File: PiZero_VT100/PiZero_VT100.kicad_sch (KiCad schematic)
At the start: 24 parts, among them J1 GPIO, J2 RS232, J3 Ext. Power max,. 9V DC/AC, J4 Mini-DIN-6, J5 to Testpins 22(DM) and TP23(D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, J6 USB_A, J7 Z80-MBC2 direct, U2 LM7805_TO220

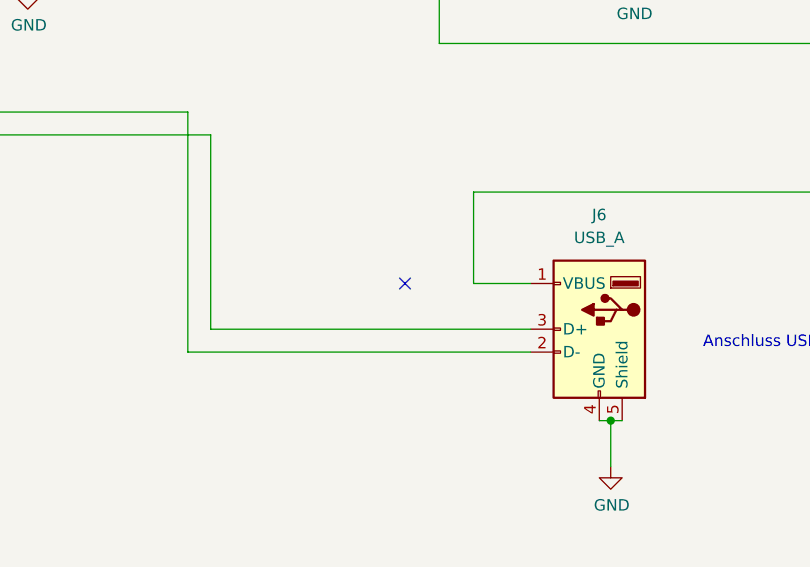
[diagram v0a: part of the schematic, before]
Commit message: Geänderte Adapterplatine mit Readme
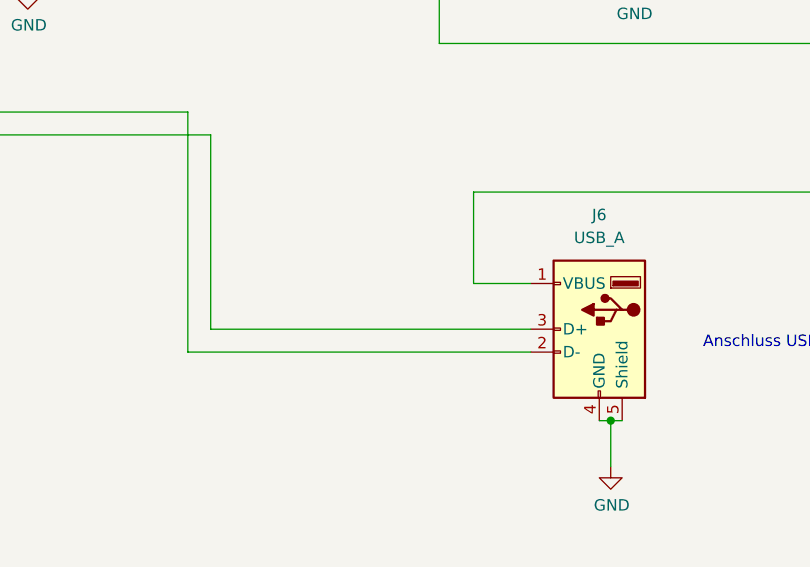
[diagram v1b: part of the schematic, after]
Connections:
- no-connect marks 36 -> 35
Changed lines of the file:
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@@
-	)
-	(no_connect
-		(at 199.39 125.73)
 	)
 	(no_connect

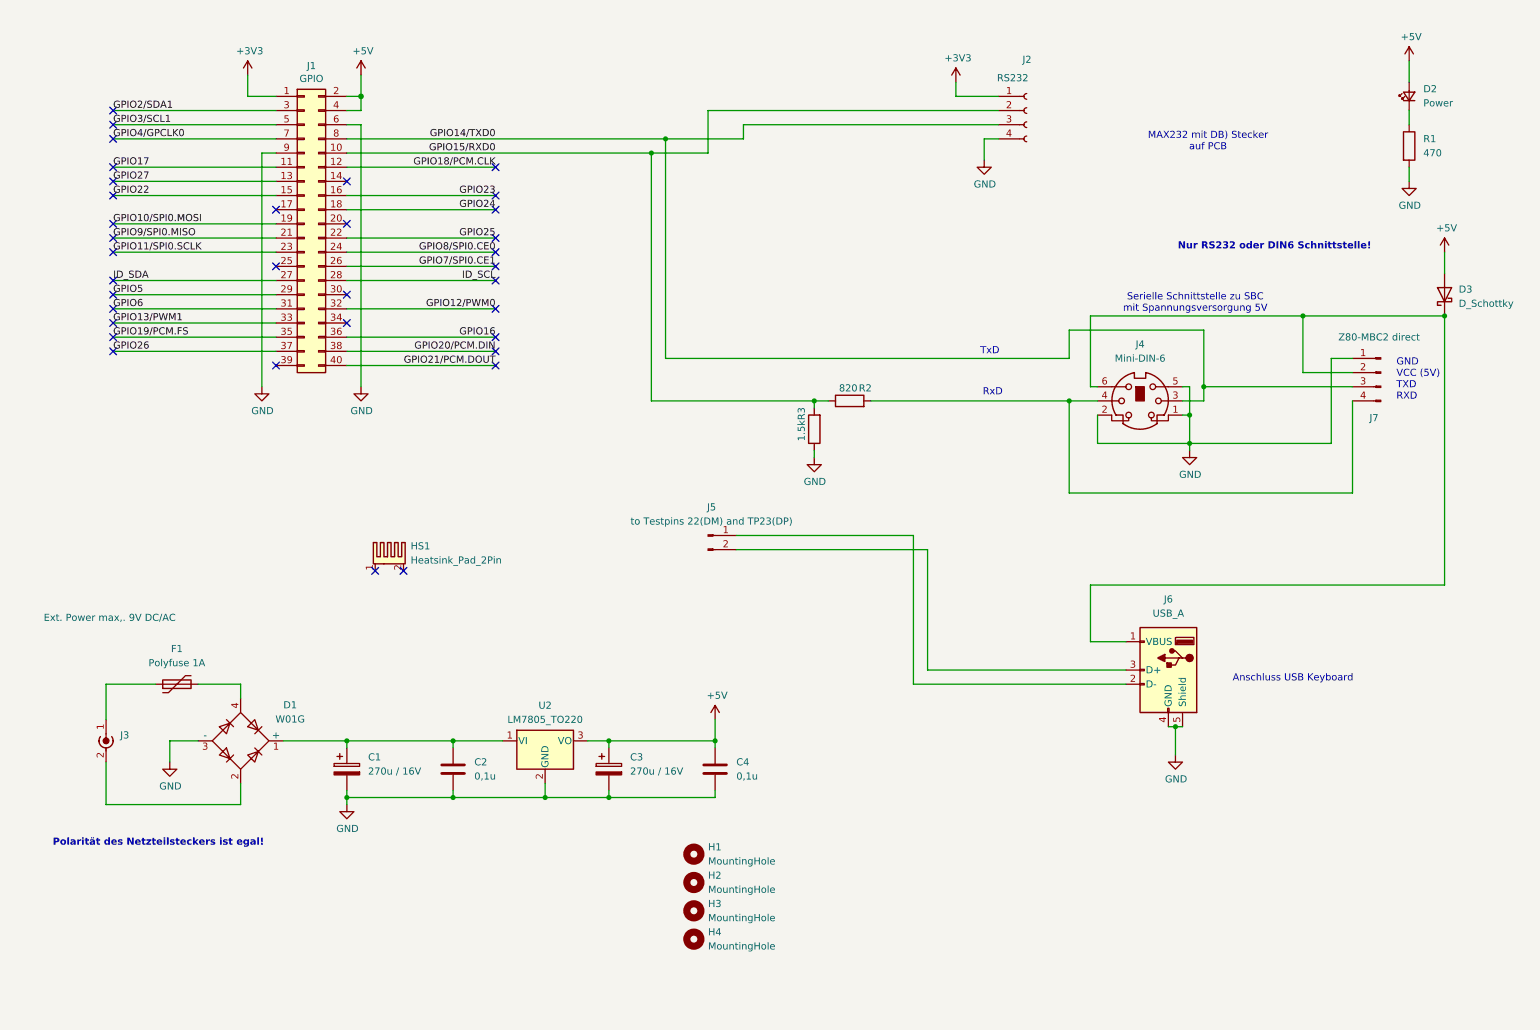
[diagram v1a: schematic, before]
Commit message: Schaltung aktualisiert Umschaltung RxD <> TxD fehlt noch
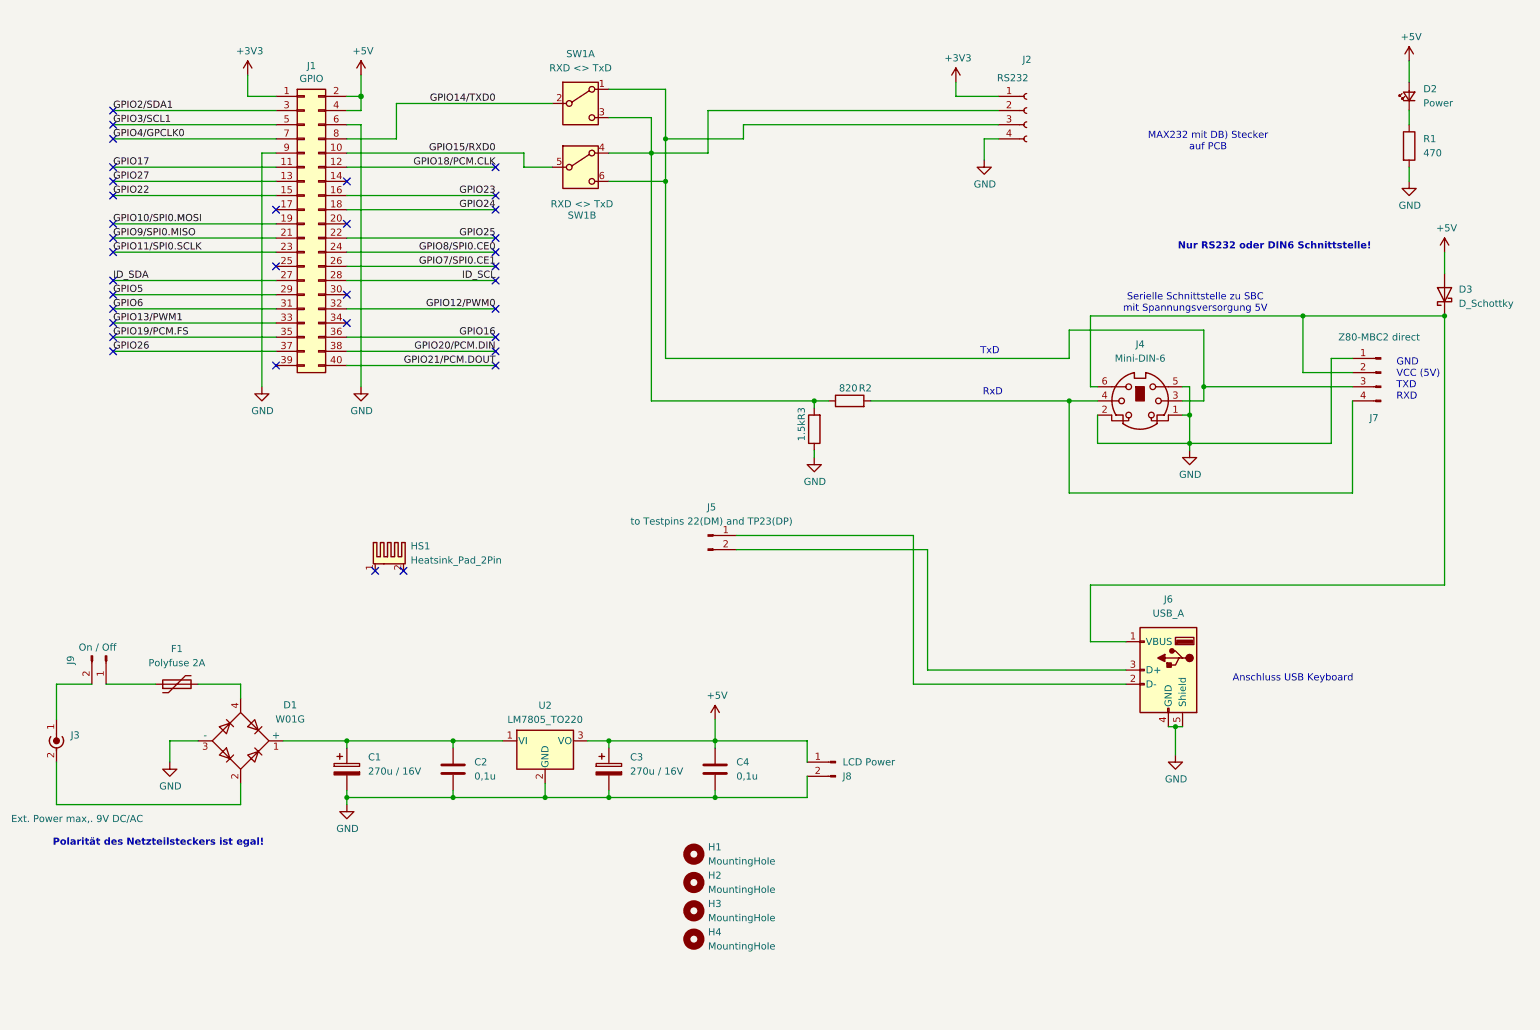
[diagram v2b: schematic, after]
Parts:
- added J8: LCD Power, Connector_PinHeader_2.54mm:PinHeader_1x02_P2.54mm_Vertical, symbol Connector:Conn_01x02_Pin
- added J9: On / Off, Connector_PinHeader_2.54mm:PinHeader_1x02_P2.54mm_Vertical, symbol Connector:Conn_01x02_Pin
- added SW1: RXD <> TxD, Button_Switch_THT:SW_CK_JS202011AQN_DPDT_Angled, symbol Switch:SW_DPDT_x2
- F1: value Polyfuse 1A -> Polyfuse 2A
- J3: footprint Connector_PinHeader_2.54mm:PinHeader_1x02_P2.54mm_Vertical -> Connector_BarrelJack:BarrelJack_GCT_DCJ200-10-A_Horizontal
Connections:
- net +5V: now also J8.1 (Pin_1)
- net GND: now also J8.2 (Pin_2)
- net GPIO14/TXD0: now also SW1.2 (B); no longer J2.3 (Pin_3), J4.3, J7.3 (Pin_3)
- net GPIO15/RXD0: now also SW1.5 (B); no longer J2.2 (Pin_2), R2.1, R3.2
- net at F1.1: now also J9.1 (Pin_1); no longer J3.1 (In)
- new net: J2.2 (Pin_2), R2.1, R3.2, SW1.3 (C), SW1.4 (A)
- new net: J2.3 (Pin_3), J4.3, J7.3 (Pin_3), SW1.1 (A), SW1.6 (C)
- new net: J3.1 (In), J9.2 (Pin_2)
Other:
- moved on the sheet: J3

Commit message: Umschalter TxD / RxD über Relais
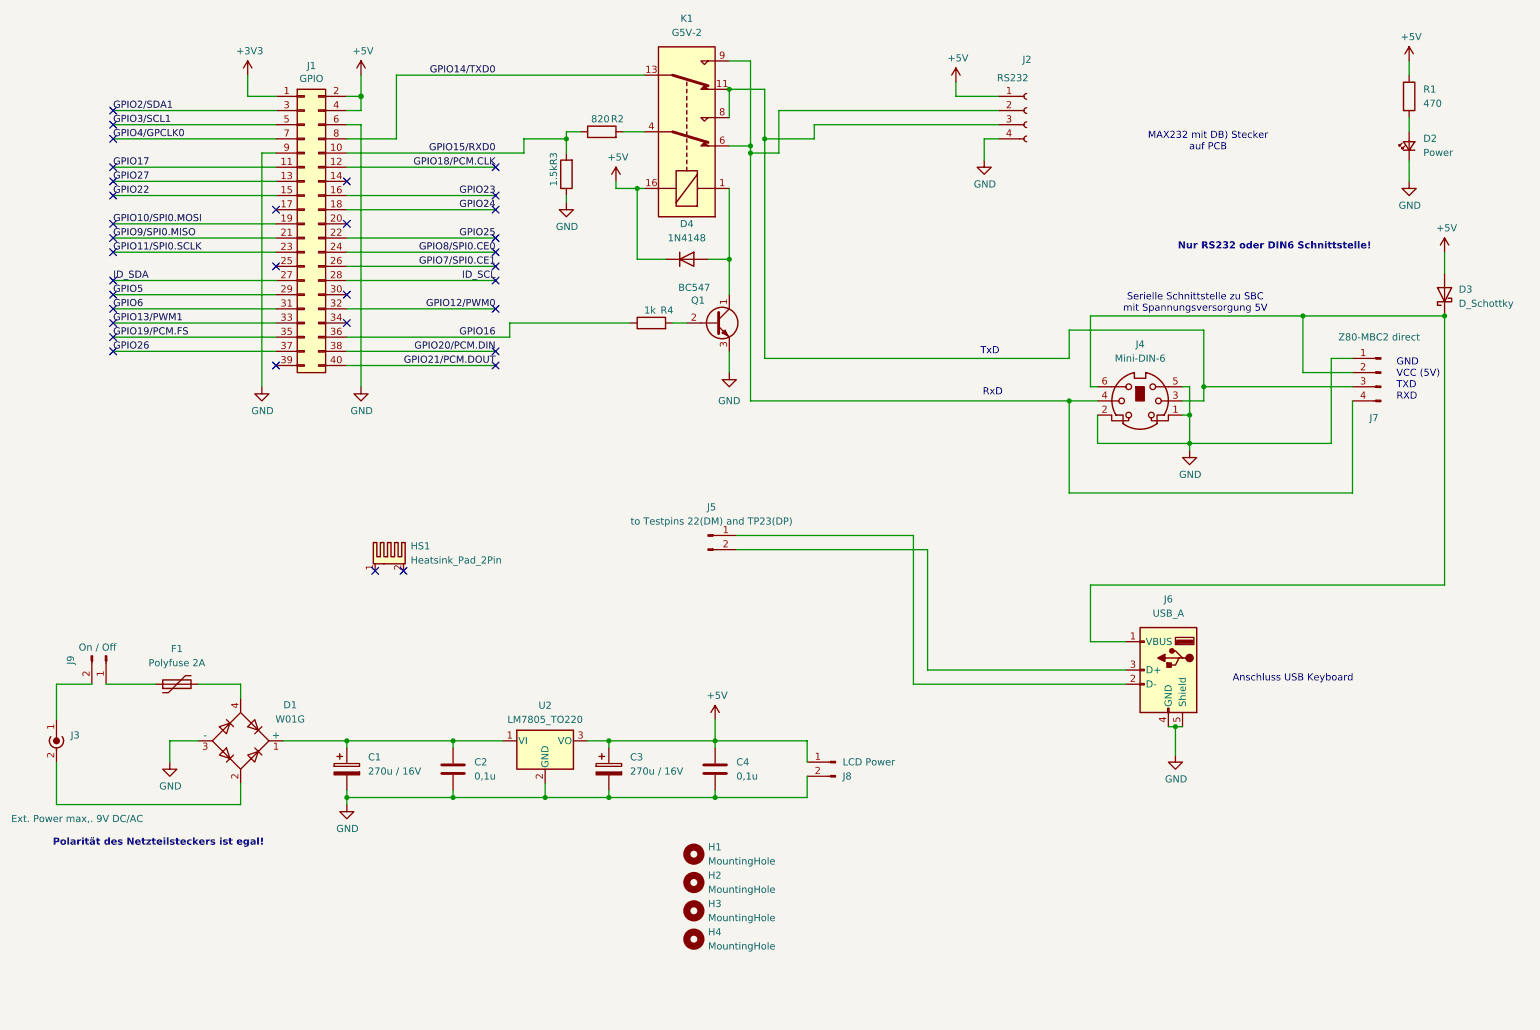
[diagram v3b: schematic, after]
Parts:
- removed SW1: RXD <> TxD, Button_Switch_THT:SW_CK_JS202011AQN_DPDT_Angled, symbol Switch:SW_DPDT_x2
- added D4: 1N4148, Diode_THT:D_A-405_P12.70mm_Horizontal, symbol Device:D
- added K1: G5V-2, Relay_THT:Relay_DPDT_Omron_G5V-2, symbol Relay:G5V-2
- added Q1: BC547, Package_TO_SOT_THT:TO-92_Wide, symbol Transistor_BJT:BC547
- added R4: 1k, Resistor_THT:R_Axial_DIN0207_L6.3mm_D2.5mm_P10.16mm_Horizontal, symbol Device:R
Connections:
- net +3V3: no longer J2.1 (Pin_1)
- net +5V: now also J2.1 (Pin_1), R1.1, D4.1 (K), K1.16; no longer D2.2 (A)
- net GND: now also D2.1 (K), Q1.3 (E); no longer R1.2
- net GPIO14/TXD0: now also K1.13
- net GPIO15/RXD0: now also R2.1, R3.2
- net GPIO16: now also R4.1
- net at J2.3 (Pin_3), J4.3, J7.3 (Pin_3): now also K1.11, K1.8
- net at J4.4, J7.4 (Pin_4): now also J2.2 (Pin_2), K1.6, K1.9; no longer R2.2
- new net: D2.2 (A), R1.2
- new net: D4.2 (A), K1.1, Q1.1 (C)
- new net: K1.4, R2.2
- new net: Q1.2 (B), R4.2
- no-connect marks 35 -> 34
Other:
- moved on the sheet: D2, R1, R2, R3

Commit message: aktualisierung des Status
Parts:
- HS1: value Heatsink_Pad_2Pin -> 6 K/W
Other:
- moved on the sheet: Q1, R4
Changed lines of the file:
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@@
 	)
 	(junction
-		(at 113.03 35.56)
+		(at 222.25 140.97)
 		(diameter 0)
 		(color 0 0 0 0)
 	)
 	(junction
-		(at 222.25 140.97)
+		(at 146.05 38.1)
 		(diameter 0)
 		(color 0 0 0 0)
 	)
 	(junction
-		(at 146.05 38.1)
+		(at 113.03 34.29)
 		(diameter 0)
 		(color 0 0 0 0)
@@
 	(wire
 		(pts
-			(xy 113.03 34.29) (xy 113.03 35.56)
+			(xy 177.8 130.81) (xy 213.36 130.81)
 		)
 		(stroke
@@
 	(wire
 		(pts
-			(xy 177.8 130.81) (xy 213.36 130.81)
+			(xy 73.66 71.12) (xy 124.46 71.12)
 		)
 		(stroke
 			(width 0)
-			(type default)
+			(type solid)
 		)
 	)
@@
 	(wire
 		(pts
+			(xy 113.03 34.29) (xy 113.03 38.1)
+		)
+		(stroke
+			(width 0)
+			(type default)
+		)
+	)
+	(wire
+		(pts
 			(xy 227.33 82.55) (xy 223.52 82.55)
 		)
@@
 	(wire
 		(pts
-			(xy 142.24 73.66) (xy 142.24 77.47)
+			(xy 142.24 76.2) (xy 142.24 80.01)
 		)
 		(stroke
@@
 	(wire
 		(pts
-			(xy 113.03 35.56) (xy 105.41 35.56)
+			(xy 113.03 34.29) (xy 105.41 34.29)
 		)
 		(stroke
@@
 	(wire
 		(pts
-			(xy 142.24 57.15) (xy 142.24 63.5)
+			(xy 142.24 57.15) (xy 142.24 66.04)
 		)
 		(stroke
@@
 	(wire
 		(pts
-			(xy 113.03 38.1) (xy 113.03 35.56)
-		)
-		(stroke
-			(width 0)
-			(type default)
-		)
-	)
-	(wire
-		(pts
 			(xy 148.59 35.56) (xy 148.59 74.93)
 		)
@@
 	(wire
 		(pts
-			(xy 102.87 68.58) (xy 102.87 71.12)
-		)
-		(stroke
-			(width 0)
-			(type default)
-		)
-	)
-	(wire
-		(pts
 			(xy 220.98 140.97) (xy 222.25 140.97)
 		)
@@
 	(wire
 		(pts
-			(xy 105.41 35.56) (xy 105.41 38.1)
+			(xy 105.41 34.29) (xy 105.41 38.1)
 		)
 		(stroke
@@
 	(wire
 		(pts
-			(xy 73.66 71.12) (xy 102.87 71.12)
-		)
-		(stroke
-			(width 0)
-			(type solid)
-		)
-	)
-	(wire
-		(pts
 			(xy 73.66 66.04) (xy 100.33 66.04)
 		)
@@
 	(wire
 		(pts
-			(xy 124.46 68.58) (xy 102.87 68.58)
-		)
-		(stroke
-			(width 0)
-			(type default)
-		)
-	)
-	(wire
-		(pts
 			(xy 54.61 133.35) (xy 54.61 135.89)
 		)
@@
 	(wire
 		(pts
-			(xy 132.08 68.58) (xy 134.62 68.58)
+			(xy 132.08 71.12) (xy 134.62 71.12)
 		)
 		(stroke
@@
 			)
 		)
-		(property "Value" "Heatsink_Pad_2Pin"
+		(property "Value" "6 K/W"
 			(at 85.09 111.1249 0)
 			(effects
@@
 	(symbol
 		(lib_id "Device:R")
-		(at 128.27 68.58 90)
+		(at 128.27 71.12 90)
 		(unit 1)
 		(exclude_from_sim no)
@@
 		(dnp no)
 		(property "Reference" "R4"
-			(at 131.064 66.294 90)
+			(at 131.064 68.834 90)
 			(effects
 				(font
@@
 		)
 		(property "Value" "1k"
-			(at 128.016 66.294 90)
+			(at 128.016 68.834 90)
 			(effects
 				(font
@@
 		)
 		(property "Footprint" "Resistor_THT:R_Axial_DIN0207_L6.3mm_D2.5mm_P10.16mm_Horizontal"
-			(at 128.27 70.358 90)
+			(at 128.27 72.898 90)
 			(effects
 				(font
@@
 		)
 		(property "Datasheet" "~"
-			(at 128.27 68.58 0)
+			(at 128.27 71.12 0)
 			(effects
 				(font
@@
 		)
 		(property "Description" "Resistor"
-			(at 128.27 68.58 0)
+			(at 128.27 71.12 0)
 			(effects
 				(font
@@
 	(symbol
 		(lib_id "power:GND")
-		(at 142.24 77.47 0)
+		(at 142.24 80.01 0)
 		(unit 1)
 		(exclude_from_sim no)
@@
 		(fields_autoplaced yes)
 		(property "Reference" "#PWR014"
-			(at 142.24 83.82 0)
+			(at 142.24 86.36 0)
 			(effects
 				(font
@@
 		)
 		(property "Value" "GND"
-			(at 142.24 82.55 0)
+			(at 142.24 85.09 0)
 			(effects
 				(font
@@
 		)
 		(property "Footprint" ""
-			(at 142.24 77.47 0)
+			(at 142.24 80.01 0)
 			(effects
 				(font
@@
 		)
 		(property "Datasheet" ""
-			(at 142.24 77.47 0)
+			(at 142.24 80.01 0)
 			(effects
 				(font
@@
 		)
 		(property "Description" "Power symbol creates a global label with name \"GND\" , ground"
-			(at 142.24 77.47 0)
+			(at 142.24 80.01 0)
 			(effects
 				(font
@@
 	(symbol
 		(lib_id "Transistor_BJT:BC547")
-		(at 139.7 68.58 0)
+		(at 139.7 71.12 0)
 		(unit 1)
 		(exclude_from_sim no)
@@
 		(dnp no)
 		(property "Reference" "Q1"
-			(at 135.382 64.516 0)
+			(at 135.382 67.056 0)
 			(effects
 				(font
@@
 		)
 		(property "Value" "BC547"
-			(at 133.096 62.23 0)
+			(at 133.096 64.77 0)
 			(effects
 				(font
@@
 		)
 		(property "Footprint" "Package_TO_SOT_THT:TO-92_Wide"
-			(at 144.78 70.485 0)
+			(at 144.78 73.025 0)
 			(effects
 				(font
@@
 		)
 		(property "Datasheet" "https://www.onsemi.com/pub/Collateral/BC550-D.pdf"
-			(at 139.7 68.58 0)
+			(at 139.7 71.12 0)
 			(effects
 				(font
@@
 		)
 		(property "Description" "0.1A Ic, 45V Vce, Small Signal NPN Transistor, TO-92"
-			(at 139.7 68.58 0)
+			(at 139.7 71.12 0)
 			(effects
 				(font

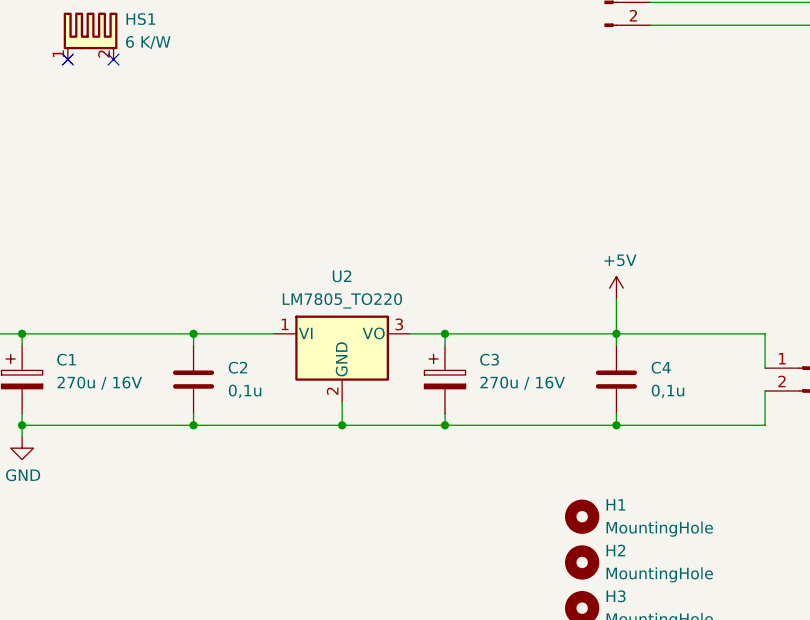
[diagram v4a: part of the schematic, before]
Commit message: LM350 eingebaut in Design
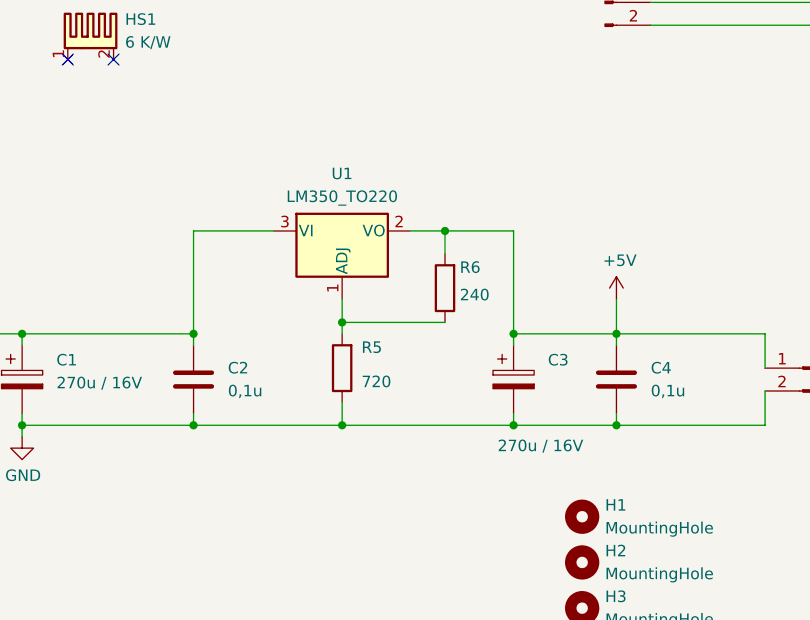
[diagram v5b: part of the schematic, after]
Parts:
- removed U2: LM7805_TO220, Package_TO_SOT_THT:TO-220-3_Vertical, symbol Regulator_Linear:LM7805_TO220
- added R5: 720, Resistor_THT:R_Axial_DIN0207_L6.3mm_D2.5mm_P10.16mm_Horizontal, symbol Device:R
- added R6: 240, Resistor_THT:R_Axial_DIN0207_L6.3mm_D2.5mm_P10.16mm_Horizontal, symbol Device:R
- added U1: LM350_TO220, Package_TO_SOT_THT:TO-220-3_Vertical, symbol Regulator_Linear:LM350_TO220
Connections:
- net +5V: now also R6.2, U1.2 (VO)
- net GND: now also R5.1
- net at C1.1, C2.1, D1.1 (+): now also U1.3 (VI)
- new net: R5.2, R6.1, U1.1 (ADJ)
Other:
- moved on the sheet: C3
